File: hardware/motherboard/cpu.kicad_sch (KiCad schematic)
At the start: 4 parts, among them U201 STM32MP157AACx

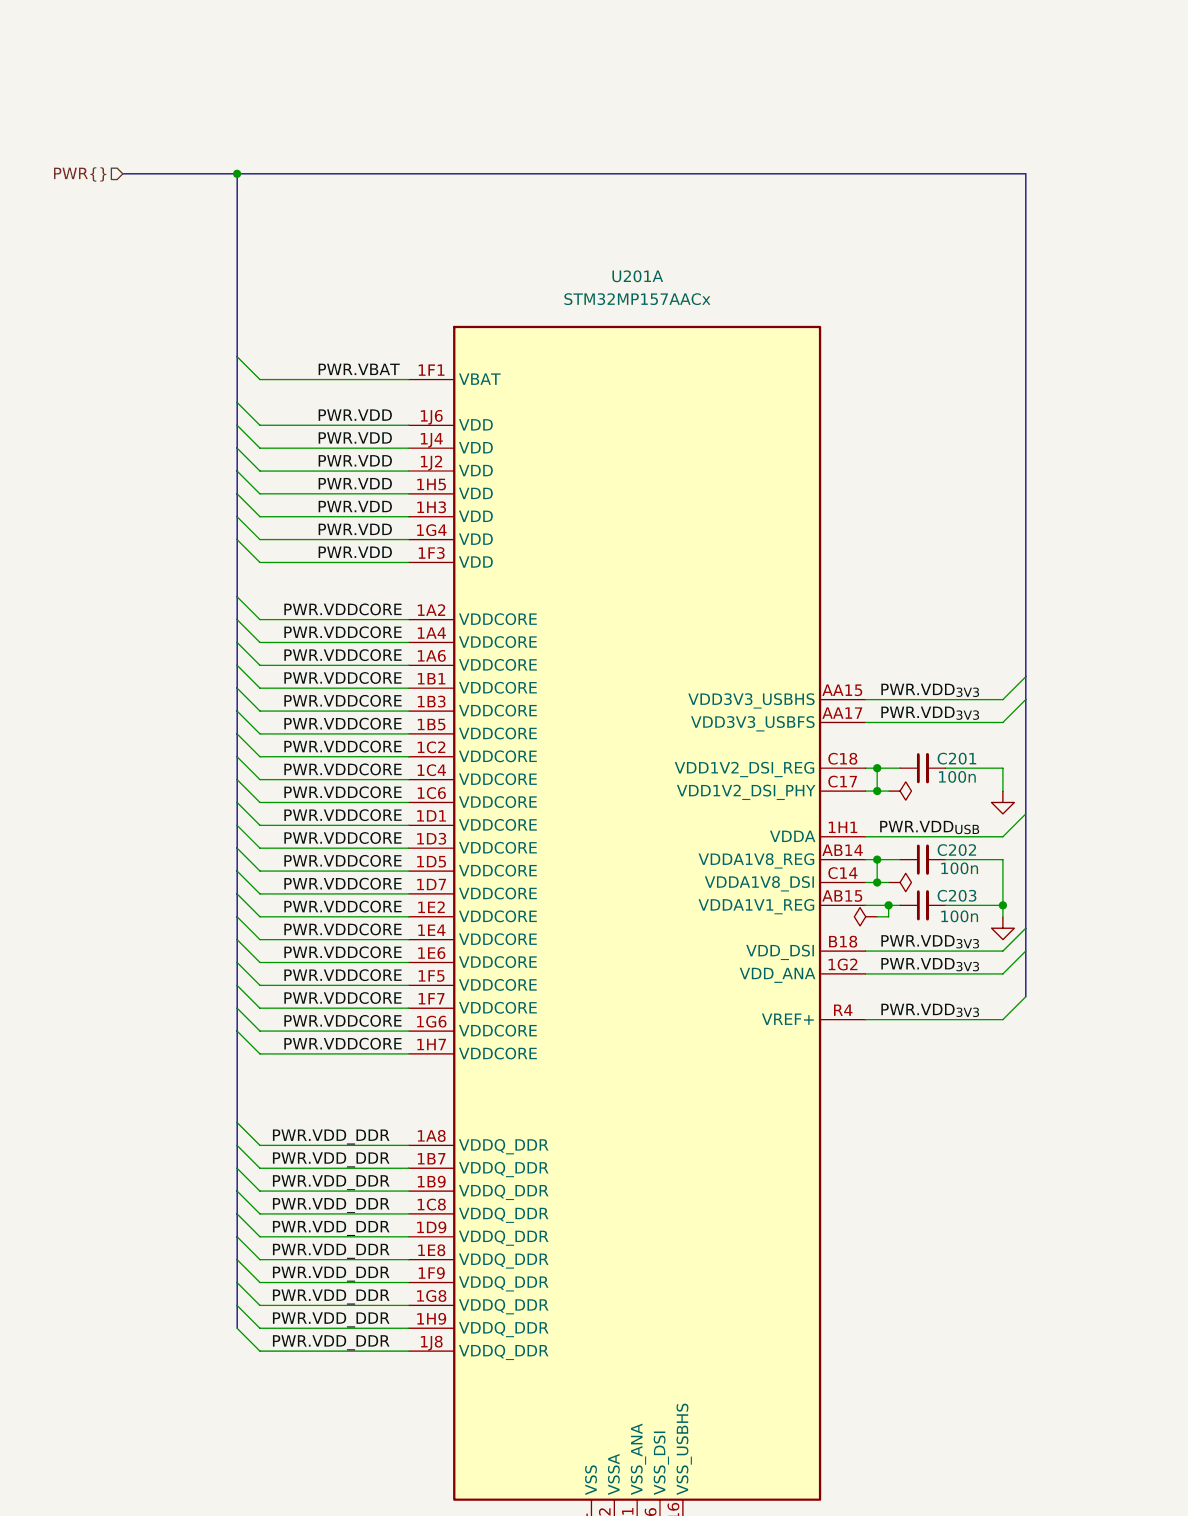
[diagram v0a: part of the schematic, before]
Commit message: Add mp157 family datasheets, fix bus errors in schematic
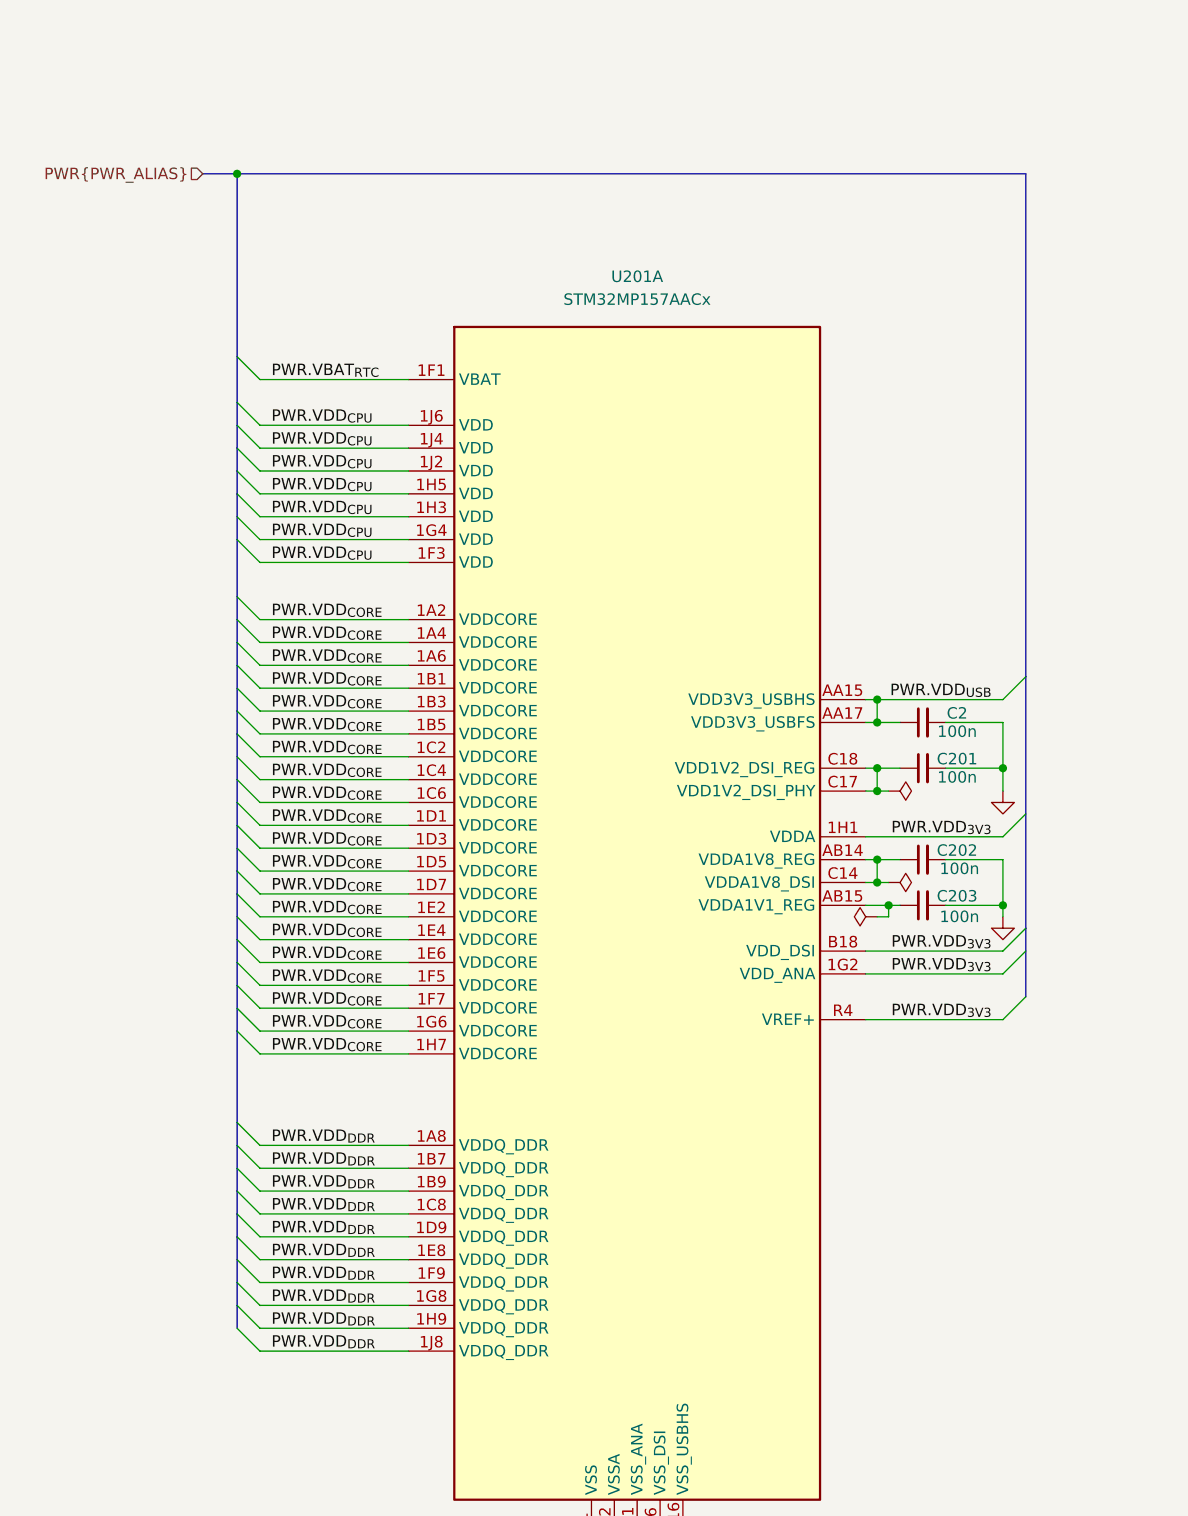
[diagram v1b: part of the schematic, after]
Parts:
- added C2: 100n, symbol Device:C_Small
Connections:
- net GND: now also C2.2
- net PWR.VDD_{3V3}: now also U201.1H1 (VDDA); no longer U201.AA15 (VDD3V3_USBHS), U201.AA17 (VDD3V3_USBFS)
- net PWR.VDD_{USB}: now also U201.AA15 (VDD3V3_USBHS), U201.AA17 (VDD3V3_USBFS), C2.1; no longer U201.1H1 (VDDA)
- net PWR.VBAT renamed PWR.VBAT_{RTC}
- net PWR.VDD renamed PWR.VDD_{CPU}
- net PWR.VDDCORE renamed PWR.VDD_{CORE}
- net PWR.VDD_DDR renamed PWR.VDD_{DDR}

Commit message: Update CPU symbol, add RAM datasheet, DDR wiring on CPU side
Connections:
- net PWR.VDD_{CPU}: now also U201.R3 (PDR_ON), U201.T3 (PDR_ON_CORE)
- net DDR.DQ20: now reaches U201.A21 (DDR_DQ20)
- net DDR.DQ23: now reaches U201.A22 (DDR_DQ23)
- net DDR.DQM3: now reaches U201.AA20 (DDR_DQM3)
- net DDR.DQ31: now reaches U201.AA22 (DDR_DQ31)
- net DDR.DQ30: now reaches U201.AA23 (DDR_DQ30)
- net DDR.DQ27: now reaches U201.AB20 (DDR_DQ27)
- net DDR.DQ26: now reaches U201.AB21 (DDR_DQ26)
- net DDR.DQSP3: now reaches U201.AB22 (DDR_DQS3P)
- net DDR.DQSN3: now reaches U201.AB23 (DDR_DQS3N)
- net DDR.VREF: now reaches U201.AC20 (DDR_VREF)
- net DDR.DQ29: now reaches U201.AC21 (DDR_DQ29)
- net DDR.DQ28: now reaches U201.AC22 (DDR_DQ28)
- net DDR.DQ19: now reaches U201.B21 (DDR_DQ19)
- net DDR.DQ16: now reaches U201.B22 (DDR_DQ16)
- net DDR.DQSN2: now reaches U201.B23 (DDR_DQS2N)
- net DDR.DQSP2: now reaches U201.C22 (DDR_DQS2P)
- net DDR.DQM2: now reaches U201.C23 (DDR_DQM2)
- net DDR.~{RESET}: now reaches U201.D20 (DDR_RESETN)
- net DDR.DQ22: now reaches U201.D21 (DDR_DQ22)
- net DDR.DQ17: now reaches U201.D22 (DDR_DQ17)
- net DDR.DQ18: now reaches U201.D23 (DDR_DQ18)
- net DDR.A7: now reaches U201.E20 (DDR_A7)
- net DDR.DQ3: now reaches U201.E21 (DDR_DQ3)
- net DDR.DQ0: now reaches U201.E22 (DDR_DQ0)
- net DDR.DQ21: now reaches U201.E23 (DDR_DQ21)
- net DDR.A13: now reaches U201.F20 (DDR_A13)
- net DDR.DQ1: now reaches U201.F22 (DDR_DQ1)
- net DDR.A9: now reaches U201.G20 (DDR_A9)
- net DDR.DQ7: now reaches U201.G21 (DDR_DQ7)
- net DDR.DQSP0: now reaches U201.G22 (DDR_DQS0P)
- net DDR.DQSN0: now reaches U201.G23 (DDR_DQS0N)
- net DDR.A5: now reaches U201.H20 (DDR_A5)
- net DDR.DQ2: now reaches U201.H21 (DDR_DQ2)
- net DDR.DQ6: now reaches U201.H22 (DDR_DQ6)
- net DDR.DQM0: now reaches U201.H23 (DDR_DQM0)
- net DDR.A2: now reaches U201.J20 (DDR_A2)
- net DDR.DQ4: now reaches U201.J21 (DDR_DQ4)
- net DDR.DQ5: now reaches U201.J22 (DDR_DQ5)
- net DDR.DTO0: now reaches U201.K20 (DDR_DTO0)
- net DDR.A3: now reaches U201.K22 (DDR_A3)
- net DDR.ZQ: now reaches U201.K23 (DDR_ZQ)
- net DDR.A0: now reaches U201.L20 (DDR_A0)
- net DDR.DTO1: now reaches U201.L21 (DDR_DTO1)
- net DDR.ODT: now reaches U201.L22 (DDR_ODT)
- net DDR.BA0: now reaches U201.L23 (DDR_BA0)
- net DDR.WEN: now reaches U201.M20 (DDR_WEN)
- net DDR.BA2: now reaches U201.M21 (DDR_BA2)
- net DDR.~{CS}: now reaches U201.M22 (DDR_CSN)
- net DDR.~{CAS}: now reaches U201.N20 (DDR_CASN)
- net DDR.~{RAS}: now reaches U201.N21 (DDR_RASN)
- net DDR.CLKP: now reaches U201.N22 (DDR_CLKP)
- net DDR.CLKN: now reaches U201.N23 (DDR_CLKN)
- net DDR.A15: now reaches U201.P20 (DDR_A15)
- net DDR.A1: now reaches U201.P22 (DDR_A1)
- net DDR.A12: now reaches U201.P23 (DDR_A12)
- net DDR.A11: now reaches U201.R20 (DDR_A11)
- net DDR.A14: now reaches U201.R21 (DDR_A14)
- net DDR.A10: now reaches U201.R22 (DDR_A10)
- net DDR.CKE: now reaches U201.T20 (DDR_CKE)
- net DDR.DQ8: now reaches U201.T21 (DDR_DQ8)
- net DDR.DQ10: now reaches U201.T22 (DDR_DQ10)
- net DDR.DQ13: now reaches U201.T23 (DDR_DQ13)
- net DDR.BA1: now reaches U201.U20 (DDR_BA1)
- net DDR.DQ9: now reaches U201.U21 (DDR_DQ9)
- net DDR.DQSP1: now reaches U201.U22 (DDR_DQS1P)
- net DDR.DQSN1: now reaches U201.U23 (DDR_DQS1N)
- net DDR.A4: now reaches U201.V20 (DDR_A4)
- net DDR.DQM1: now reaches U201.V22 (DDR_DQM1)
- net DDR.A6: now reaches U201.W20 (DDR_A6)
- net DDR.DQ11: now reaches U201.W21 (DDR_DQ11)
- net DDR.DQ14: now reaches U201.W22 (DDR_DQ14)
- net DDR.DQ12: now reaches U201.W23 (DDR_DQ12)
- net DDR.ATO: now reaches U201.Y19 (DDR_ATO)
- net DDR.A8: now reaches U201.Y20 (DDR_A8)
- net DDR.DQ15: now reaches U201.Y21 (DDR_DQ15)
- net DDR.DQ25: now reaches U201.Y22 (DDR_DQ25)
- net DDR.DQ24: now reaches U201.Y23 (DDR_DQ24)
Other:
- moved on the sheet: C2, C201, C202, C203, U201A, U201B, U201C, U201D, U201E

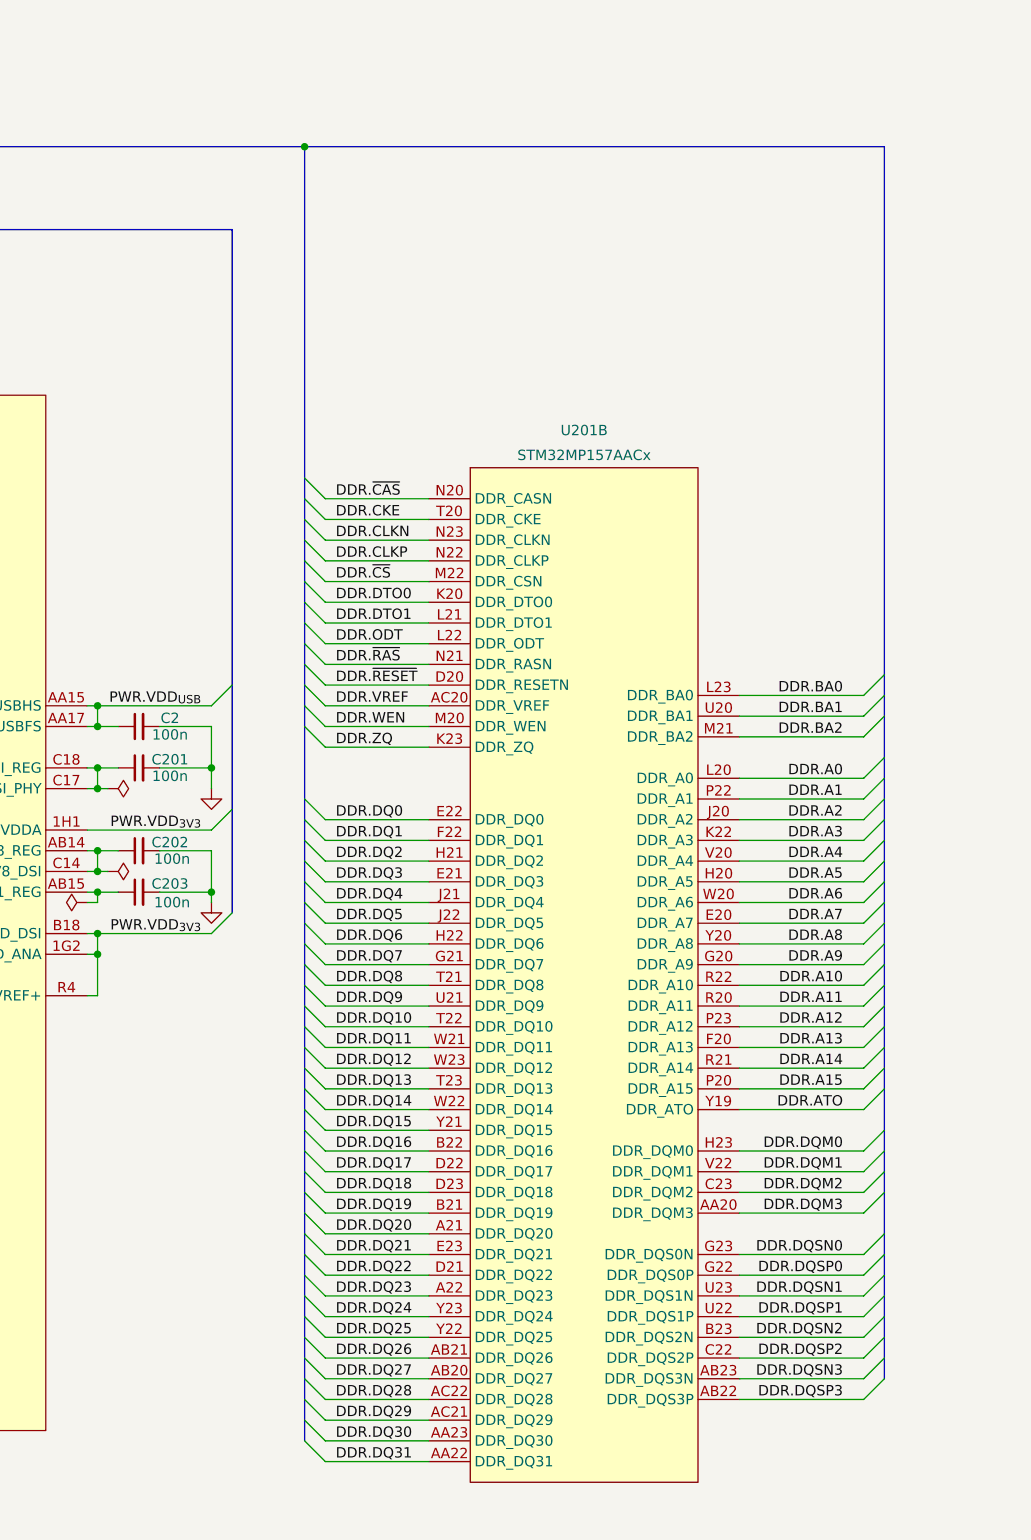
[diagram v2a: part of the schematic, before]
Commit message: Add RAM, models, connect RAM
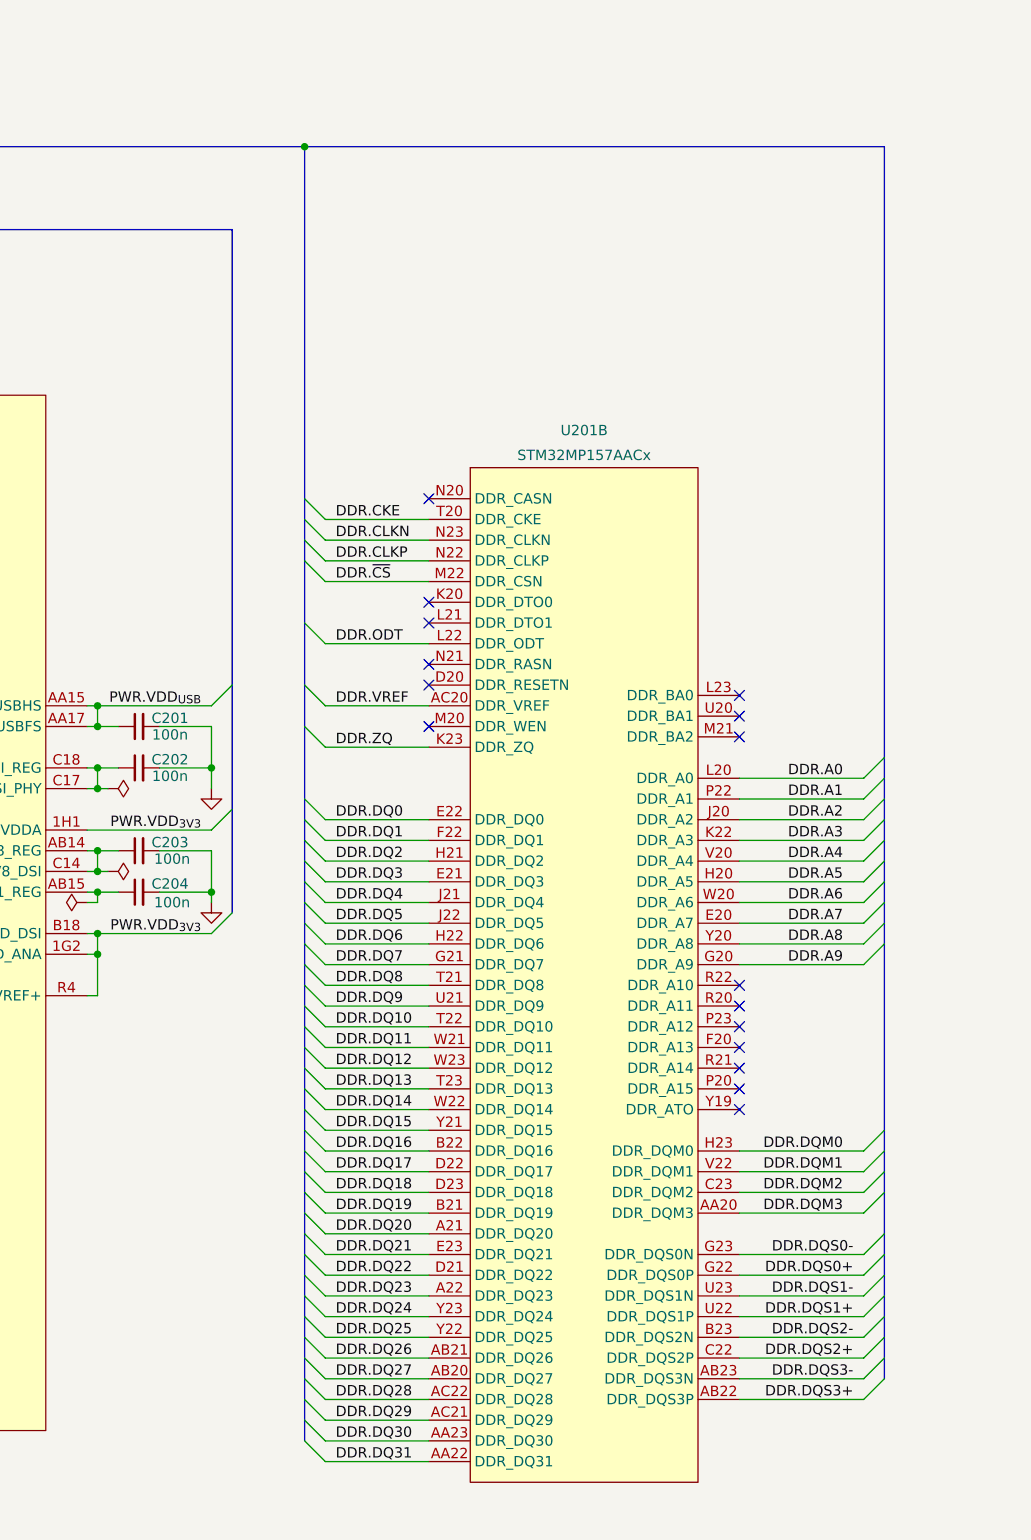
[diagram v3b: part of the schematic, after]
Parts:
- renumbered C2 to C201, C201 to C202, C202 to C203, C203 to C204
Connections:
- net DDR.A10: no longer names the net of U201.R22 (DDR_A10)
- net DDR.A11: no longer names the net of U201.R20 (DDR_A11)
- net DDR.A12: no longer names the net of U201.P23 (DDR_A12)
- net DDR.A13: no longer names the net of U201.F20 (DDR_A13)
- net DDR.A14: no longer names the net of U201.R21 (DDR_A14)
- net DDR.A15: no longer names the net of U201.P20 (DDR_A15)
- net DDR.ATO: no longer names the net of U201.Y19 (DDR_ATO)
- net DDR.BA0: no longer names the net of U201.L23 (DDR_BA0)
- net DDR.BA1: no longer names the net of U201.U20 (DDR_BA1)
- net DDR.BA2: no longer names the net of U201.M21 (DDR_BA2)
- net DDR.DQSN0 renamed DDR.DQS0-
- net DDR.DQSN1 renamed DDR.DQS1-
- net DDR.DQSN2 renamed DDR.DQS2-
- net DDR.DQSN3 renamed DDR.DQS3-
- net DDR.DQSP0 renamed DDR.DQS0+
- net DDR.DQSP1 renamed DDR.DQS1+
- net DDR.DQSP2 renamed DDR.DQS2+
- net DDR.DQSP3 renamed DDR.DQS3+
- net DDR.DTO0: no longer names the net of U201.K20 (DDR_DTO0)
- net DDR.DTO1: no longer names the net of U201.L21 (DDR_DTO1)
- net DDR.WEN: no longer names the net of U201.M20 (DDR_WEN)
- net DDR.~{CAS}: no longer names the net of U201.N20 (DDR_CASN)
- net DDR.~{RAS}: no longer names the net of U201.N21 (DDR_RASN)
- net DDR.~{RESET}: no longer names the net of U201.D20 (DDR_RESETN)
- no-connect marks 0 -> 16

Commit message: Start routing RAM, add more docs
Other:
- moved on the sheet: C201, C202, C203, C204, U201A, U201B, U201C, U201D, U201E
